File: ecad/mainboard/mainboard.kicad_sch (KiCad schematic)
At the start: 26 parts, among them J1 IR LED, J2 IR Diode, M1 Left N20 Motor, M2 Right N20 Motor, U1 LM393

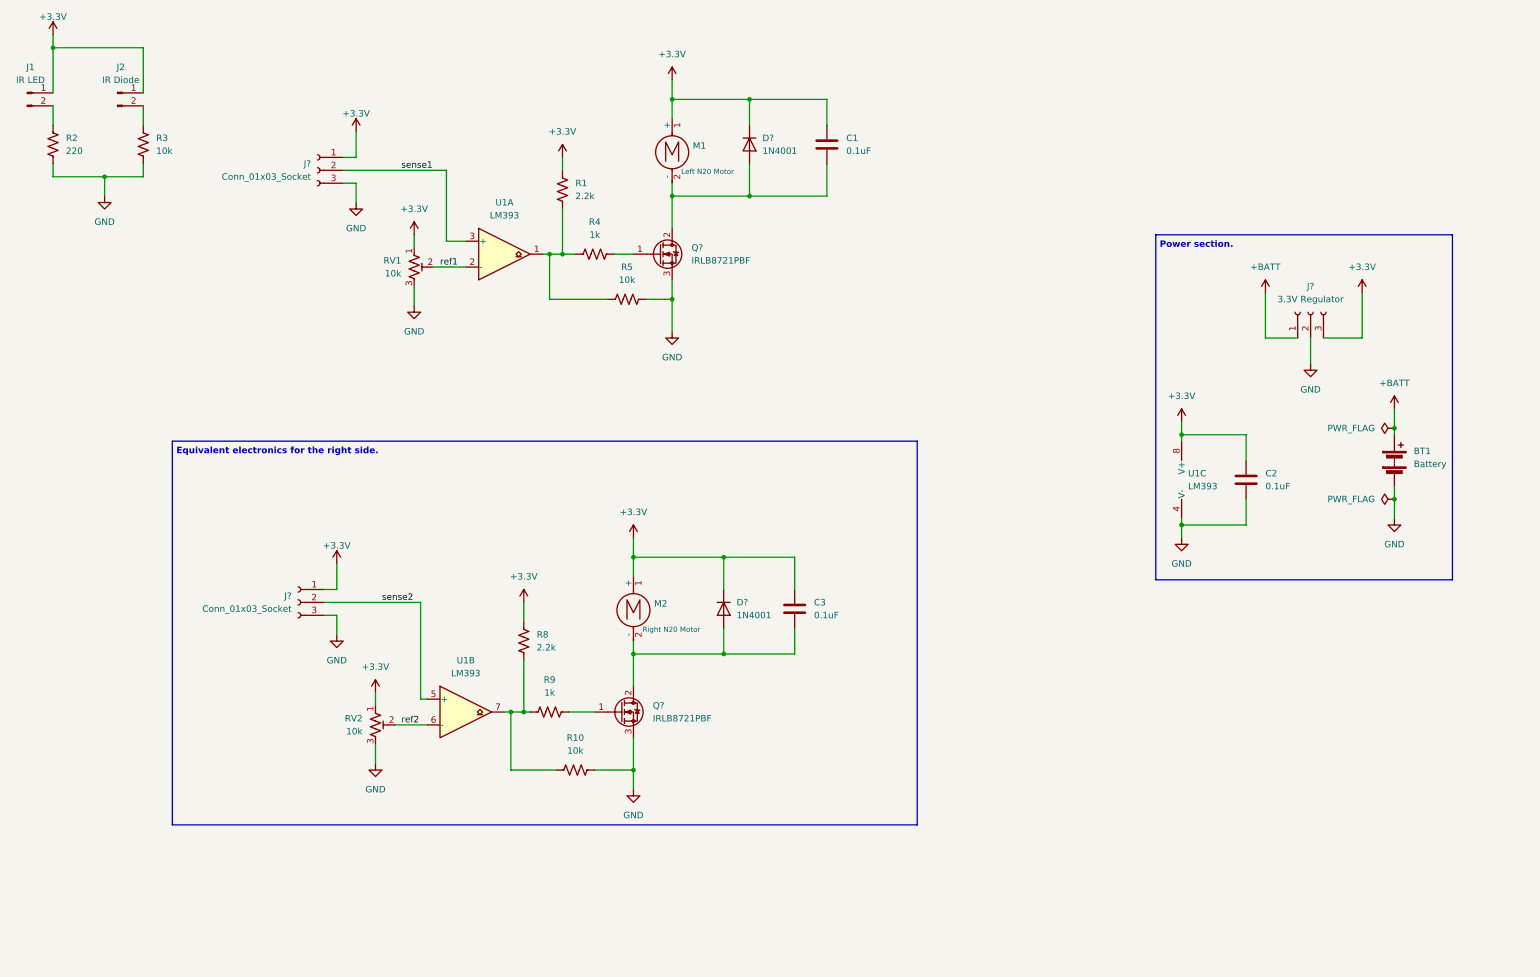
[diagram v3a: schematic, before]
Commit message: ecad: update footprints
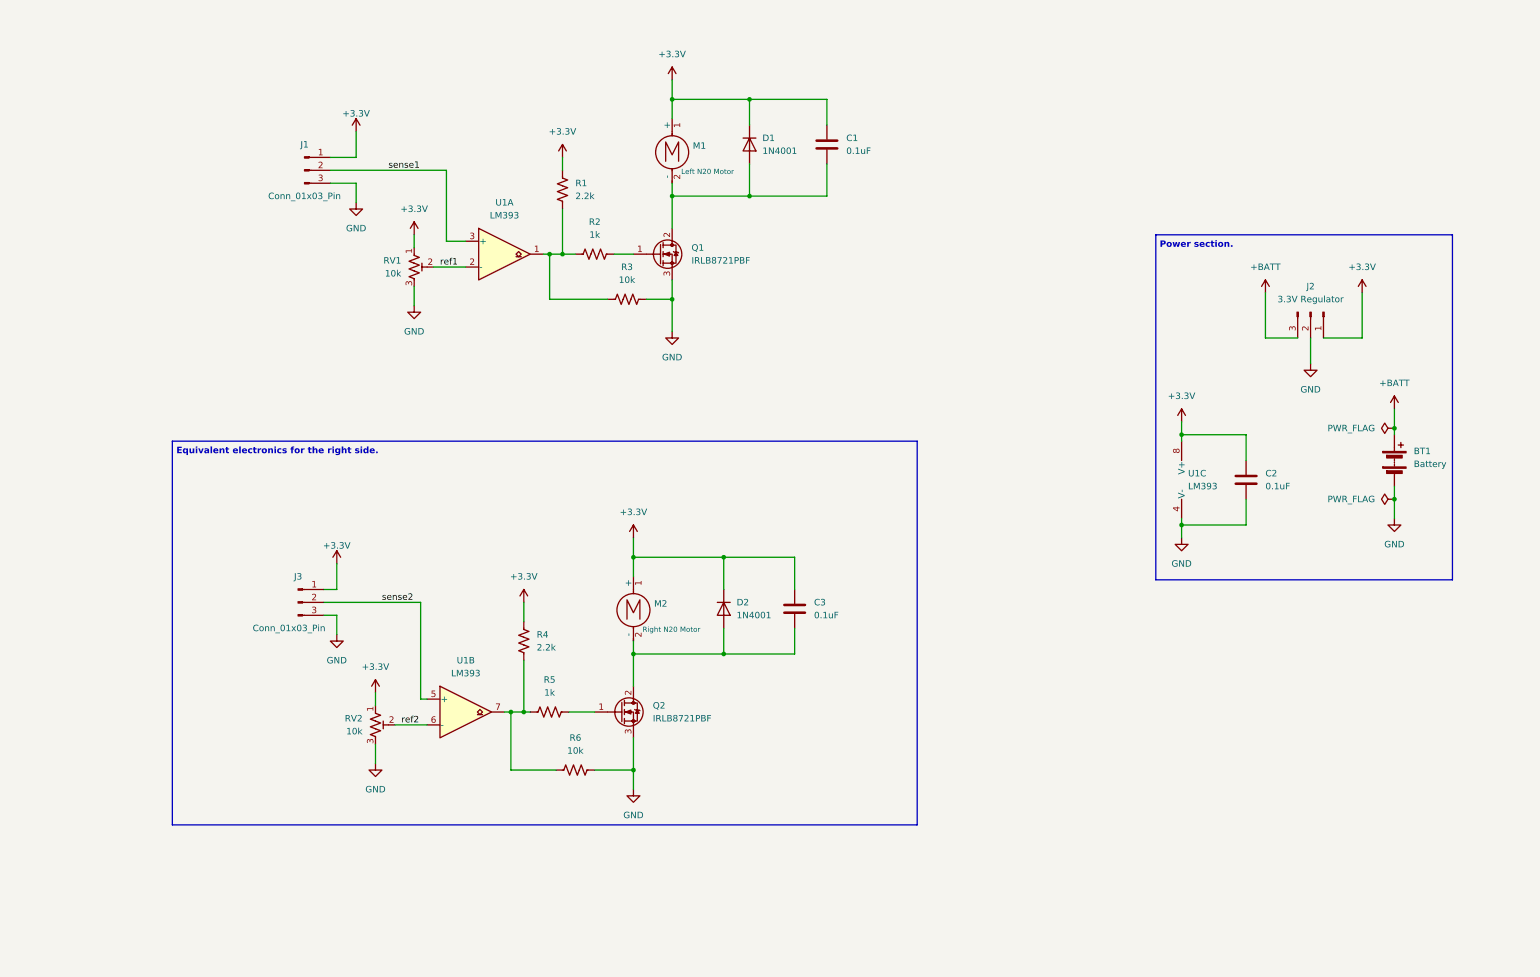
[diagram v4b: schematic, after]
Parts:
- removed J1: IR LED, Connector_JST:JST_XH_S2B-XH-A_1x02_P2.50mm_Horizontal, symbol Connector:Conn_01x02_Pin
- removed J2: IR Diode, Connector_JST:JST_XH_S2B-XH-A_1x02_P2.50mm_Horizontal, symbol Connector:Conn_01x02_Pin
- removed J?: 3.3V Regulator, symbol Connector:Conn_01x03_Socket
- removed R2: 220, Resistor_SMD:R_0603_1608Metric, symbol Device:R_US
- removed R3: 10k, Resistor_SMD:R_0603_1608Metric, symbol Device:R_US
- added J2: 3.3V Regulator, Connector_PinHeader_2.54mm:PinHeader_1x03_P2.54mm_Vertical, symbol Connector:Conn_01x03_Pin
- C1, C2, C3: footprint Capacitor_SMD:C_0402_1005Metric -> Capacitor_THT:C_Radial_D4.0mm_H7.0mm_P1.50mm
- J1, J3: renamed from J?; value Conn_01x03_Socket -> Conn_01x03_Pin; footprint (none) -> Connector_PinHeader_2.54mm:PinHeader_1x03_P2.54mm_Horizontal; symbol Connector:Conn_01x03_Socket -> Connector:Conn_01x03_Pin
- R1: footprint Resistor_SMD:R_0603_1608Metric -> Resistor_THT:R_Axial_DIN0207_L6.3mm_D2.5mm_P7.62mm_Horizontal
- R2: renamed from R4; footprint Resistor_SMD:R_0603_1608Metric -> Resistor_THT:R_Axial_DIN0207_L6.3mm_D2.5mm_P7.62mm_Horizontal
- R3: renamed from R5; footprint Resistor_SMD:R_0603_1608Metric -> Resistor_THT:R_Axial_DIN0207_L6.3mm_D2.5mm_P7.62mm_Horizontal
- R4: renamed from R8; footprint Resistor_SMD:R_0603_1608Metric -> Resistor_THT:R_Axial_DIN0207_L6.3mm_D2.5mm_P7.62mm_Horizontal
- R5: renamed from R9; footprint Resistor_SMD:R_0603_1608Metric -> Resistor_THT:R_Axial_DIN0207_L6.3mm_D2.5mm_P7.62mm_Horizontal
- R6: renamed from R10; footprint Resistor_SMD:R_0603_1608Metric -> Resistor_THT:R_Axial_DIN0207_L6.3mm_D2.5mm_P7.62mm_Horizontal
- U1: footprint Package_SO:SOIC-8_3.9x4.9mm_P1.27mm -> Package_DIP:DIP-8_W7.62mm_Socket
- gave numbers to parts that had none: 4
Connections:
- net +3.3V: now also J2.1 (Pin_1)
- net +BATT: now also J2.3 (Pin_3)
- net GND: now also J2.2 (Pin_2)

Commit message: update schematic footprints
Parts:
- BT1: footprint TerminalBlock_4Ucon:TerminalBlock_4Ucon_1x02_P3.50mm_Vertical -> TerminalBlock_MetzConnect:TerminalBlock_MetzConnect_Type059_RT06302HBWC_1x02_P3.50mm_Horizontal
- M1, M2: footprint Connector_JST:JST_ZH_B2B-ZR_1x02_P1.50mm_Vertical -> Connector_Wire:SolderWire-0.5sqmm_1x02_P4.8mm_D0.9mm_OD2.3mm
